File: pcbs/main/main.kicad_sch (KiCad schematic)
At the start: 14 parts

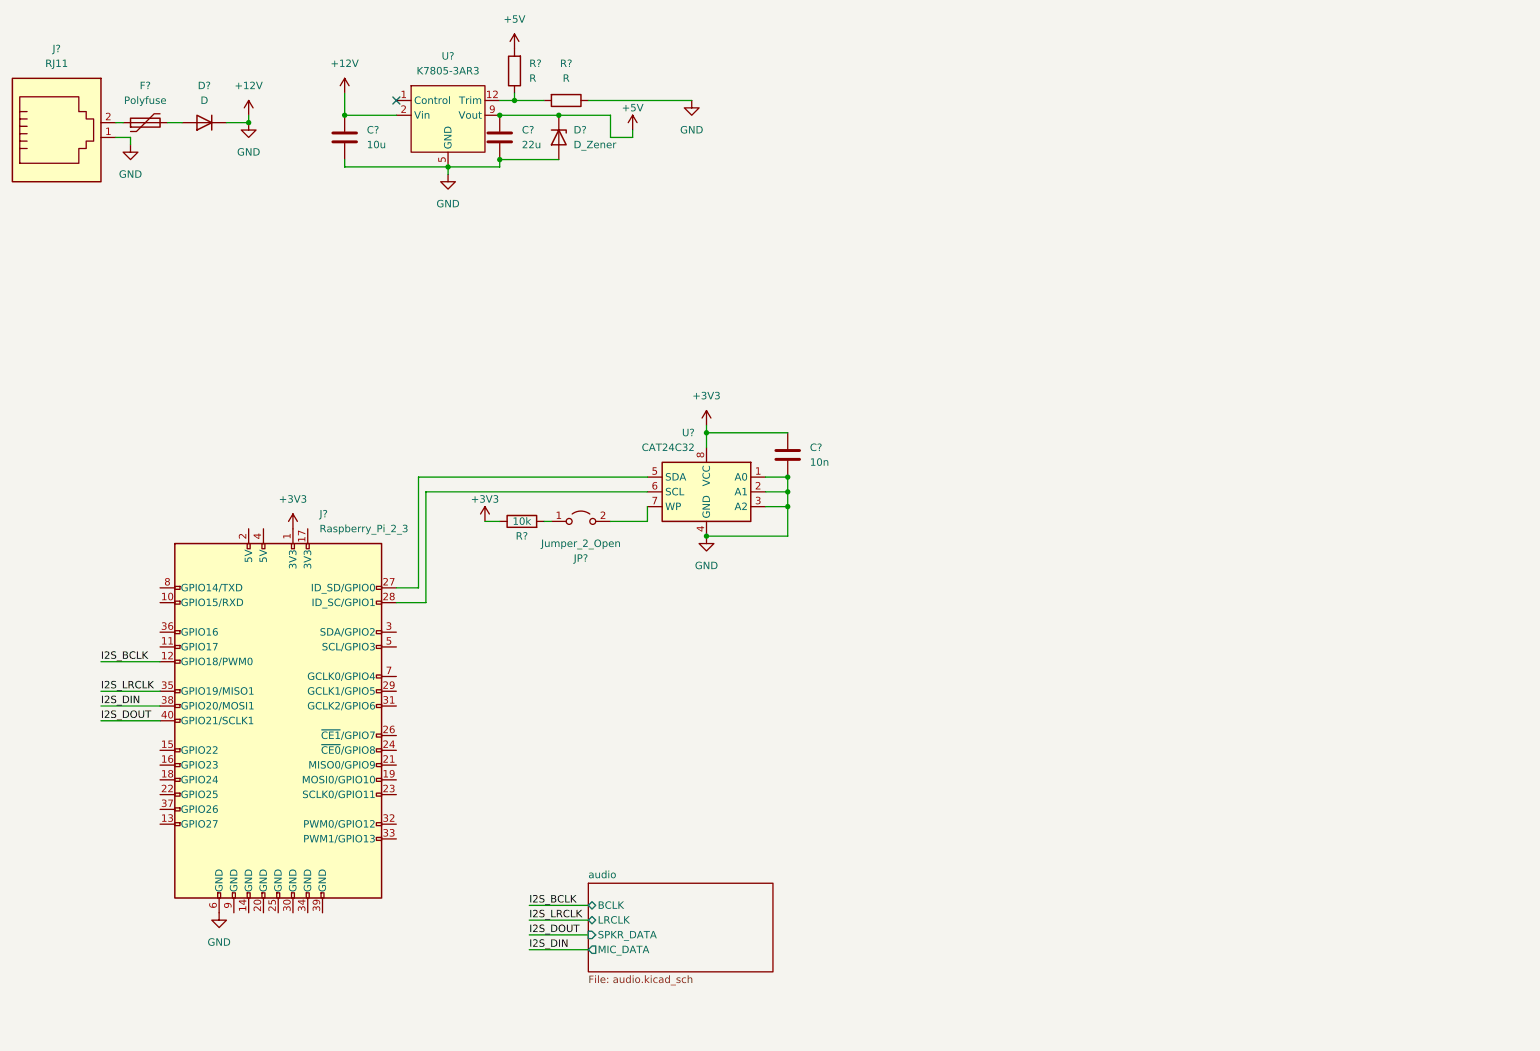
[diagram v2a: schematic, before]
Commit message: Add connector for button PCB, add IR LEDs
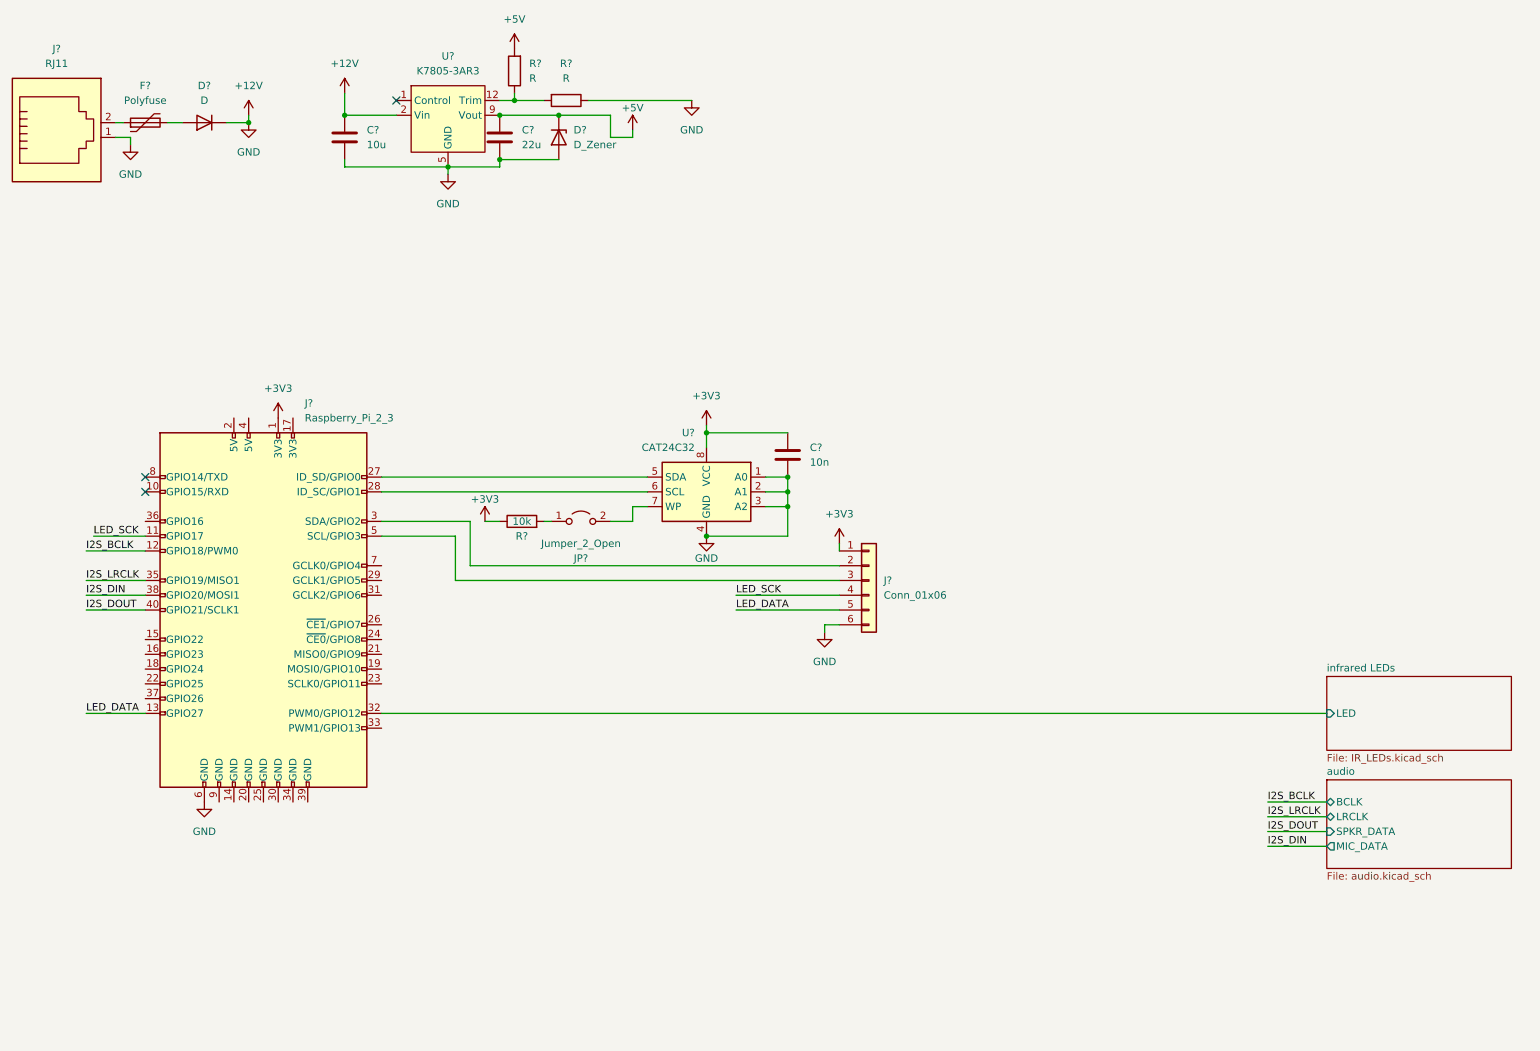
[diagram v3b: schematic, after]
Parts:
- added J?: Conn_01x06, symbol Connector_Generic:Conn_01x06
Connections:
- net +12V: now also J?.6 (Pin_6)
- net +3V3: now also J?.1 (Pin_1)
- net LED_SCK: now reaches J?.11 (GPIO17)
- net LED_SCK: now also J?.4 (Pin_4)
- net LED_DATA: now reaches J?.13 (GPIO27)
- net LED_DATA: now also J?.5 (Pin_5)
- net at J?.3 (SDA/GPIO2): now also J?.2 (Pin_2)
- net infrared LEDs/LED: now reaches J?.32 (PWM0/GPIO12)
- net at J?.5 (SCL/GPIO3): now also J?.3 (Pin_3)
- no-connect marks 1 -> 3
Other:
- added sheet infrared LEDs (IR_LEDs.kicad_sch)
- moved on the sheet: J?

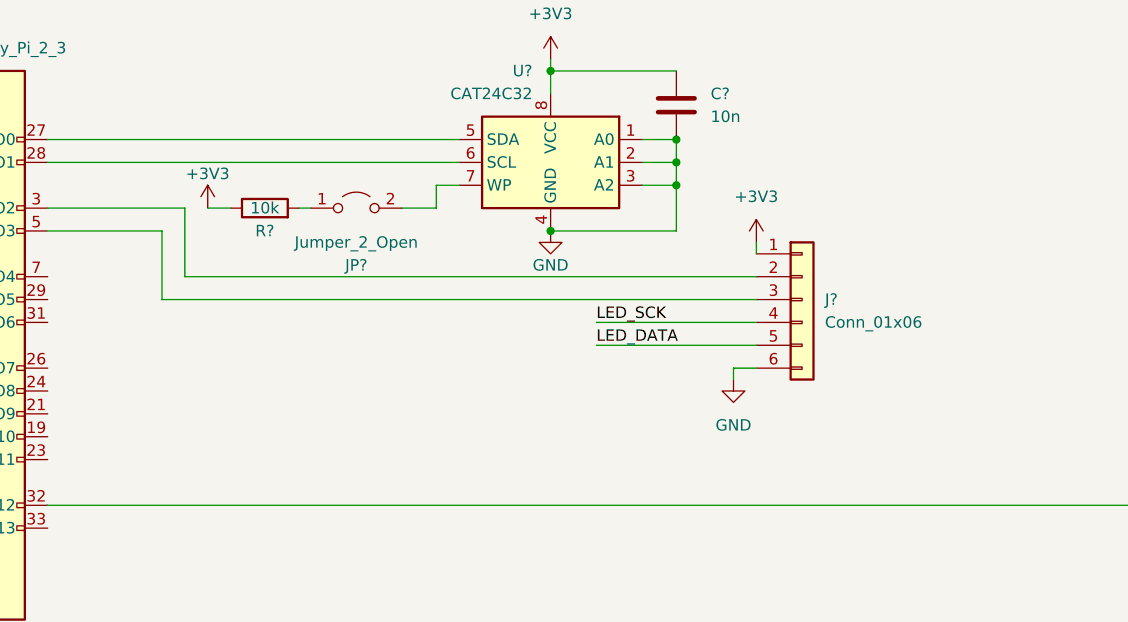
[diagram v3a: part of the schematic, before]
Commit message: Add separate PCB for button with capacitive controller.
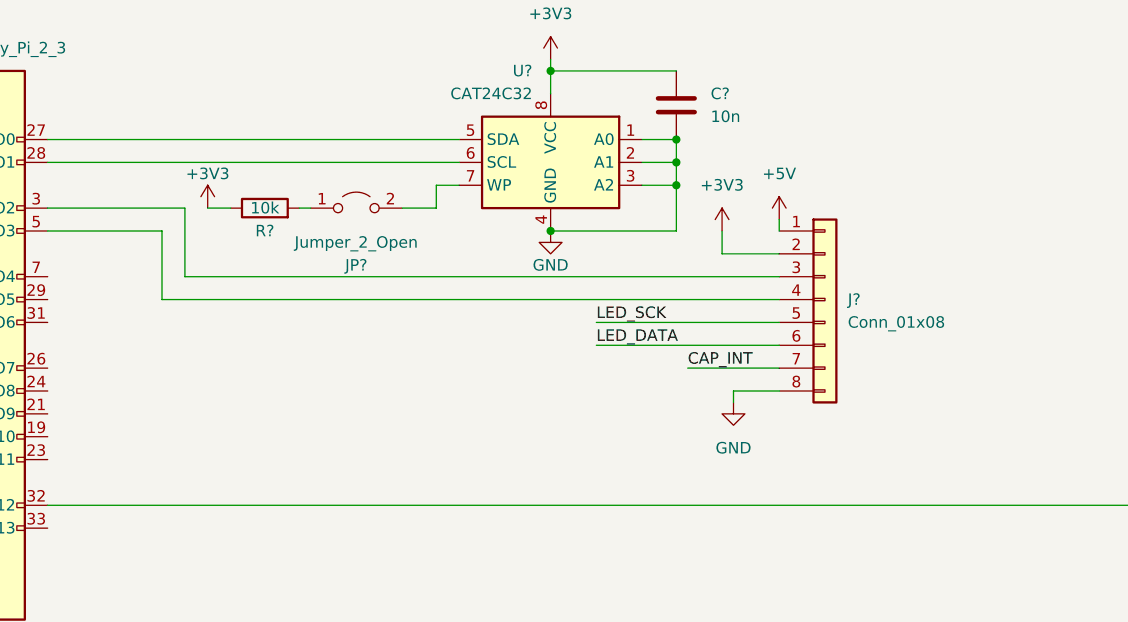
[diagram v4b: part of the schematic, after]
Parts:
- removed J?: Conn_01x06, symbol Connector_Generic:Conn_01x06
- added J?: Conn_01x08, symbol Connector_Generic:Conn_01x08
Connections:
- net +12V: now also J?.8 (Pin_8)
- net +3V3: now also J?.2 (Pin_2)
- net +5V: now also J?.1 (Pin_1)
- net LED_DATA: now also J?.6 (Pin_6)
- net LED_SCK: now also J?.5 (Pin_5)
- net at J?.3 (SDA/GPIO2): now also J?.3 (Pin_3)
- net at J?.5 (SCL/GPIO3): now also J?.4 (Pin_4)
- new net CAP_INT: J?.7 (Pin_7)
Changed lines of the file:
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@@
     (stroke (width 0) (type default) (color 0 0 0 0))
   )
-  (wire (pts (xy 163.83 120.65) (xy 163.83 119.38))
+  (wire (pts (xy 163.83 123.19) (xy 163.83 121.92))
     (stroke (width 0) (type default) (color 0 0 0 0))
   )
@@
     (stroke (width 0) (type default) (color 0 0 0 0))
   )
-  (wire (pts (xy 163.83 119.38) (xy 166.37 119.38))
+  (wire (pts (xy 163.83 121.92) (xy 168.91 121.92))
     (stroke (width 0) (type default) (color 0 0 0 0))
   )
@@
     (stroke (width 0) (type default) (color 0 0 0 0))
   )
-  (wire (pts (xy 166.37 105.41) (xy 166.37 106.68))
-    (stroke (width 0) (type default) (color 0 0 0 0))
-  )
   (wire (pts (xy 36.83 111.76) (xy 46.99 111.76))
     (stroke (width 0) (type default) (color 0 0 0 0))
@@
     (stroke (width 0) (type default) (color 0 0 0 0))
   )
-  (wire (pts (xy 102.87 109.22) (xy 166.37 109.22))
+  (wire (pts (xy 102.87 109.22) (xy 168.91 109.22))
     (stroke (width 0) (type default) (color 0 0 0 0))
   )
@@
     (stroke (width 0) (type default) (color 0 0 0 0))
   )
-  (wire (pts (xy 100.33 111.76) (xy 166.37 111.76))
+  (wire (pts (xy 100.33 111.76) (xy 168.91 111.76))
     (stroke (width 0) (type default) (color 0 0 0 0))
   )
@@
     (stroke (width 0) (type default) (color 0 0 0 0))
   )
+  (wire (pts (xy 168.91 102.87) (xy 168.91 104.14))
+    (stroke (width 0) (type default) (color 0 0 0 0))
+  )
   (wire (pts (xy 107.95 40.64) (xy 107.95 39.37))
     (stroke (width 0) (type default) (color 0 0 0 0))
@@
     (stroke (width 0) (type default) (color 0 0 0 0))
   )
-  (wire (pts (xy 148.59 114.3) (xy 166.37 114.3))
+  (wire (pts (xy 148.59 114.3) (xy 168.91 114.3))
     (stroke (width 0) (type default) (color 0 0 0 0))
   )
@@
     (stroke (width 0) (type default) (color 0 0 0 0))
   )
+  (wire (pts (xy 168.91 106.68) (xy 162.56 106.68))
+    (stroke (width 0) (type default) (color 0 0 0 0))
+  )
   (wire (pts (xy 130.81 35.56) (xy 130.81 34.29))
     (stroke (width 0) (type default) (color 0 0 0 0))
@@
     (stroke (width 0) (type default) (color 0 0 0 0))
   )
-  (wire (pts (xy 148.59 116.84) (xy 166.37 116.84))
+  (wire (pts (xy 148.59 116.84) (xy 168.91 116.84))
     (stroke (width 0) (type default) (color 0 0 0 0))
   )
@@
     (stroke (width 0) (type default) (color 0 0 0 0))
   )
+  (wire (pts (xy 162.56 106.68) (xy 162.56 104.14))
+    (stroke (width 0) (type default) (color 0 0 0 0))
+  )
+  (wire (pts (xy 158.75 119.38) (xy 168.91 119.38))
+    (stroke (width 0) (type default) (color 0 0 0 0))
+  )
   (wire (pts (xy 153.67 99.06) (xy 157.48 99.06))
     (stroke (width 0) (type default) (color 0 0 0 0))
@@
   )
   (label "LED_SCK" (at 38.1 104.14 0)
+    (effects (font (size 1.27 1.27)) (justify left bottom))
+  )
+  (label "CAP_INT" (at 158.75 119.38 0)
     (effects (font (size 1.27 1.27)) (justify left bottom))
   )
@@
     (pin "2")
   )
+  (symbol (lib_id "power:+5V") (at 168.91 102.87 0) (unit 1)
+    (in_bom yes) (on_board yes) (fields_autoplaced)
+    (property "Reference" "#PWR?" (id 0) (at 168.91 106.68 0)
+      (effects (font (size 1.27 1.27)) hide)
+    )
+    (property "Value" "+5V" (id 1) (at 168.91 97.79 0))
+    (property "Footprint" "" (id 2) (at 168.91 102.87 0)
+      (effects (font (size 1.27 1.27)) hide)
+    )
+    (property "Datasheet" "" (id 3) (at 168.91 102.87 0)
+      (effects (font (size 1.27 1.27)) hide)
+    )
+    (pin "1")
+  )
   (symbol (lib_id "Device:D_Zener") (at 118.11 35.56 270) (unit 1)
     (in_bom yes) (on_board yes) (fields_autoplaced)
@@
     (pin "1")
   )
-  (symbol (lib_id "Connector_Generic:Conn_01x06") (at 171.45 111.76 0) (unit 1)
-    (in_bom yes) (on_board yes) (fields_autoplaced)
-    (property "Reference" "J?" (id 0) (at 173.99 111.7599 0)
-      (effects (font (size 1.27 1.27)) (justify left))
-    )
-    (property "Value" "Conn_01x06" (id 1) (at 173.99 114.2999 0)
-      (effects (font (size 1.27 1.27)) (justify left))
-    )
-    (property "Footprint" "" (id 2) (at 171.45 111.76 0)
-      (effects (font (size 1.27 1.27)) hide)
-    )
-    (property "Datasheet" "~" (id 3) (at 171.45 111.76 0)
+  (symbol (lib_id "Connector_Generic:Conn_01x08") (at 173.99 111.76 0) (unit 1)
+    (in_bom yes) (on_board yes) (fields_autoplaced)
+    (property "Reference" "J?" (id 0) (at 176.53 111.7599 0)
+      (effects (font (size 1.27 1.27)) (justify left))
+    )
+    (property "Value" "Conn_01x08" (id 1) (at 176.53 114.2999 0)
+      (effects (font (size 1.27 1.27)) (justify left))
+    )
+    (property "Footprint" "" (id 2) (at 173.99 111.76 0)
+      (effects (font (size 1.27 1.27)) hide)
+    )
+    (property "Datasheet" "~" (id 3) (at 173.99 111.76 0)
       (effects (font (size 1.27 1.27)) hide)
     )
@@
     (pin "5")
     (pin "6")
+    (pin "7")
+    (pin "8")
   )
   (symbol (lib_id "Device:R") (at 111.76 101.6 90) (unit 1)
@@
     (pin "2")
   )
-  (symbol (lib_id "power:+3V3") (at 166.37 105.41 0) (unit 1)
-    (in_bom yes) (on_board yes) (fields_autoplaced)
-    (property "Reference" "#PWR?" (id 0) (at 166.37 109.22 0)
-      (effects (font (size 1.27 1.27)) hide)
-    )
-    (property "Value" "+3V3" (id 1) (at 166.37 100.33 0))
-    (property "Footprint" "" (id 2) (at 166.37 105.41 0)
-      (effects (font (size 1.27 1.27)) hide)
-    )
-    (property "Datasheet" "" (id 3) (at 166.37 105.41 0)
+  (symbol (lib_id "power:+3V3") (at 162.56 104.14 0) (unit 1)
+    (in_bom yes) (on_board yes) (fields_autoplaced)
+    (property "Reference" "#PWR?" (id 0) (at 162.56 107.95 0)
+      (effects (font (size 1.27 1.27)) hide)
+    )
+    (property "Value" "+3V3" (id 1) (at 162.56 99.06 0))
+    (property "Footprint" "" (id 2) (at 162.56 104.14 0)
+      (effects (font (size 1.27 1.27)) hide)
+    )
+    (property "Datasheet" "" (id 3) (at 162.56 104.14 0)
       (effects (font (size 1.27 1.27)) hide)
     )
@@
     (pin "2")
   )
-  (symbol (lib_id "power:GND") (at 163.83 120.65 0) (unit 1)
-    (in_bom yes) (on_board yes) (fields_autoplaced)
-    (property "Reference" "#PWR?" (id 0) (at 163.83 127 0)
-      (effects (font (size 1.27 1.27)) hide)
-    )
-    (property "Value" "GND" (id 1) (at 163.83 125.73 0))
-    (property "Footprint" "" (id 2) (at 163.83 120.65 0)
-      (effects (font (size 1.27 1.27)) hide)
-    )
-    (property "Datasheet" "" (id 3) (at 163.83 120.65 0)
+  (symbol (lib_id "power:GND") (at 163.83 123.19 0) (unit 1)
+    (in_bom yes) (on_board yes) (fields_autoplaced)
+    (property "Reference" "#PWR?" (id 0) (at 163.83 129.54 0)
+      (effects (font (size 1.27 1.27)) hide)
+    )
+    (property "Value" "GND" (id 1) (at 163.83 128.27 0))
+    (property "Footprint" "" (id 2) (at 163.83 123.19 0)
+      (effects (font (size 1.27 1.27)) hide)
+    )
+    (property "Datasheet" "" (id 3) (at 163.83 123.19 0)
       (effects (font (size 1.27 1.27)) hide)
     )
@@
       (reference "#PWR?") (unit 1) (value "GND") (footprint "")
     )
+    (path "/127d8f75-641b-48e7-9b4f-72c870ac87dd"
+      (reference "#PWR?") (unit 1) (value "+5V") (footprint "")
+    )
     (path "/c9bcbb20-bce5-48eb-aaa8-469331798139/18c0c5ea-e708-416d-a9a7-2a2227831eb3"
       (reference "#PWR?") (unit 1) (value "GND") (footprint "")
@@
       (reference "F?") (unit 1) (value "Polyfuse") (footprint "")
     )
-    (path "/358aee86-9240-4717-bc25-9e7e2599468a"
-      (reference "J?") (unit 1) (value "Conn_01x06") (footprint "")
+    (path "/2305ad78-9786-4c09-8492-3a264bf34a2c"
+      (reference "J?") (unit 1) (value "Conn_01x08") (footprint "")
     )
     (path "/b831411d-850e-4769-933d-eb36367747f9"
